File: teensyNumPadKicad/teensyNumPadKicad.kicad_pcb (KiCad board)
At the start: 2 copper layers, 82.6 x 177 mm, 59 parts, among them J1 KCDX-5S-S2, U1 Teensy++2.0_(C)

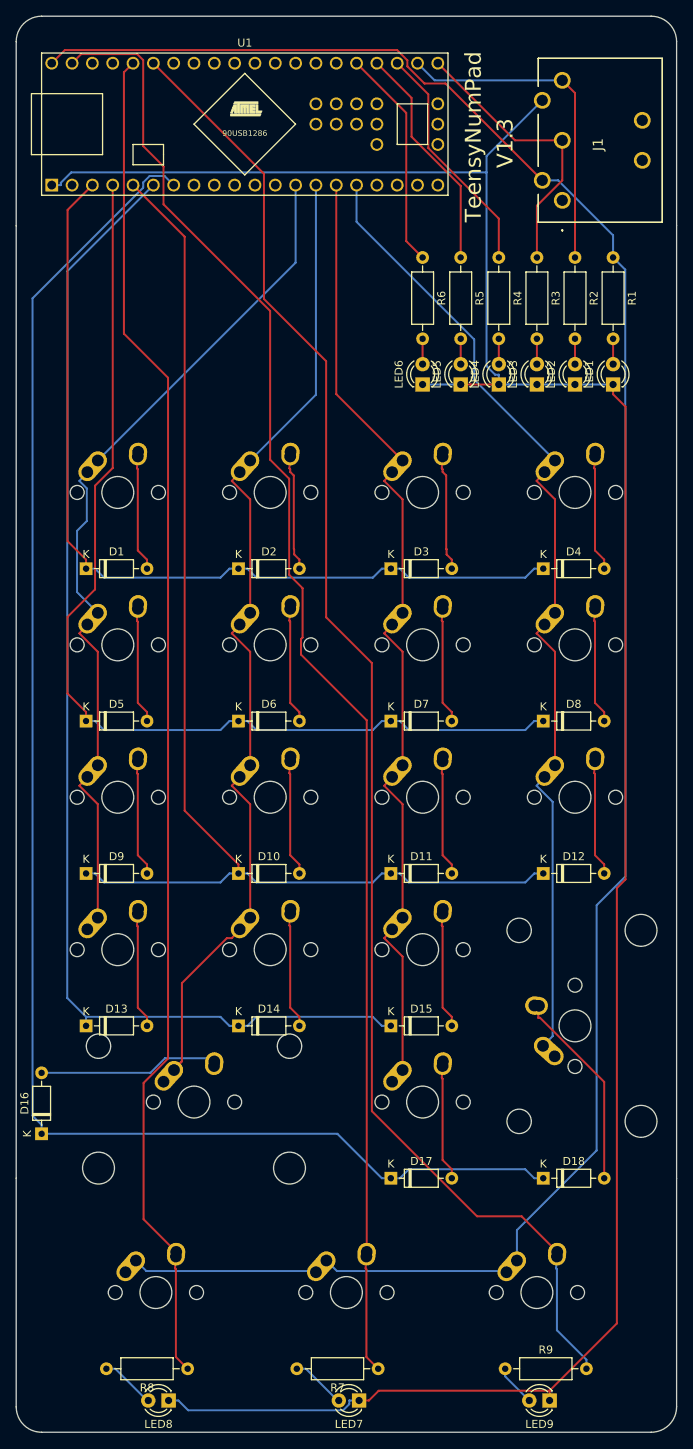
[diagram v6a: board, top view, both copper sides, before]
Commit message: Update to use MX-LED footprints where required
Use MX-LED footprints for MX-19, MX20 + MX21.
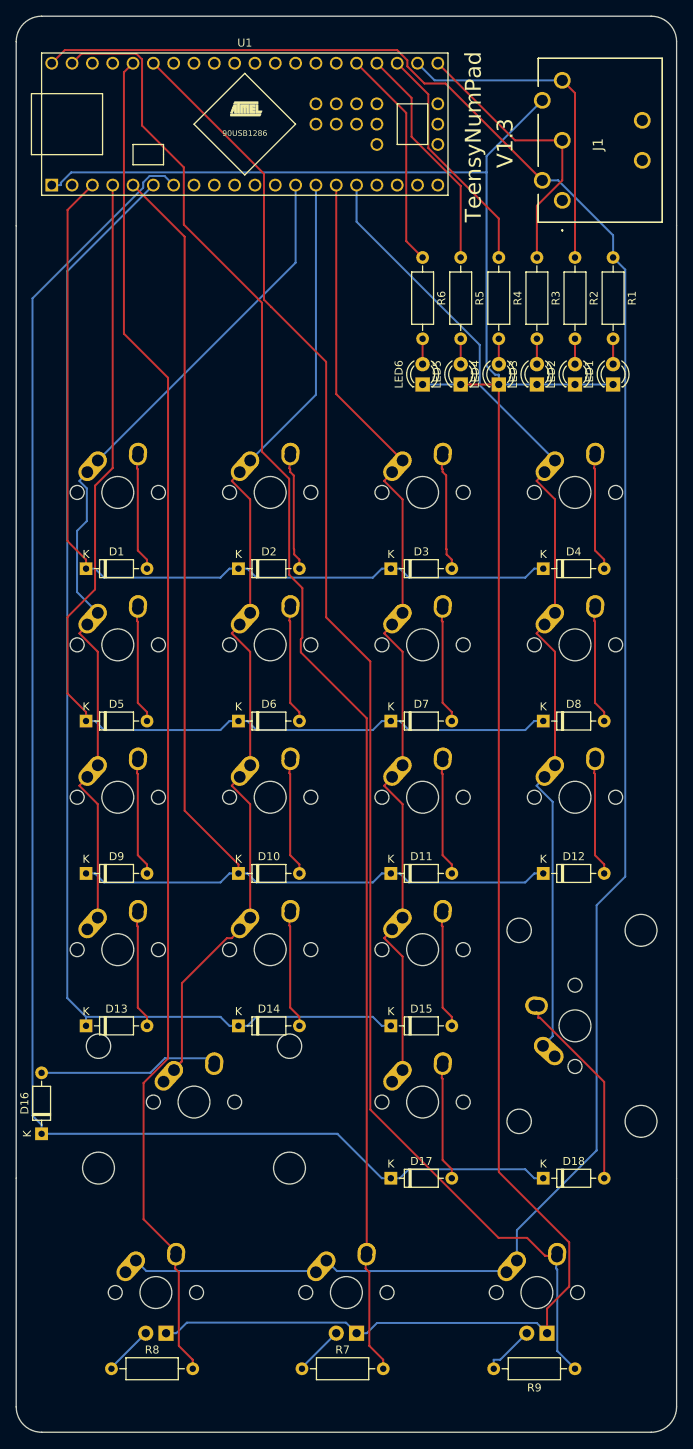
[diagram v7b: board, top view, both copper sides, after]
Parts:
- removed LED7, LED8, LED9: LED, LED_THT:LED_D3.0mm
- MX19, MX20, MX21: value MX-NoLED -> MX-LED; footprint MX_Alps_Hybrid:MX-1.25U-NoLED -> MX_Alps_Hybrid:MX-1.25U
- moved R7 9.53 mm to (104.0, 198.4), turned to 0 degrees
- moved R8 9.52 mm to (80.2, 198.4), turned to 0 degrees
- moved R9 8.73 mm to (138.1, 198.4), turned to 180 degrees
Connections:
- R7 pad 1: LAMI -> Net-(MX19-Pad3)
- R7 pad 2: Net-(LED7-Pad2) -> LAMI
- R8 pad 1: CTRL -> Net-(MX20-Pad3)
- R8 pad 2: Net-(LED8-Pad2) -> CTRL
- R9 pad 1: Net-(LED9-Pad2) -> RAMI
- R9 pad 2: RAMI -> Net-(MX21-Pad3)
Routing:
- net GND: track 299.3 -> 291.4 mm
- net Net-(LED7-Pad2): track 6.88 -> 0.00 mm
- net Net-(LED8-Pad2): track 6.88 -> 0.00 mm
- net Net-(MX21-Pad3): track 0.00 -> 6.63 mm
- net Net-(MX19-Pad3): track 0.00 -> 6.22 mm
- net Net-(MX20-Pad3): track 0.00 -> 6.22 mm
- net Net-(LED9-Pad2): track 5.22 -> 0.00 mm
